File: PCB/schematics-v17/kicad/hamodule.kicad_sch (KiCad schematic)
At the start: 82 parts, among them J1 2604-1104, J10 EspSense, J11 Conn_01x02_Male, J12 NoCon, J2 2604-1102, J3 USB_C_Receptacle_USB2.0, J4 ESP Relays, J5 Current Jumper, J6 GND 3.3V, J7 Conn_01x02, J8 Current Jumper, J9 2604-1104, K1 PCN-105D, K2 PCN-105D, K3 PCN-105D, K4 PCN-105D, Q1 SS8050-SMD, Q2 SS8050, SW1 EN, SW2 IO0, U1 ULN2003A, U2 ESP32-WROOM-32E, U4 LD1117AV33_TO220, U5 MCP9700T-ETT, U6 LDA210-PDIP, U7 LDA210-PDIP, U8 CP2102N-A01-GQFN28

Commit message: adding gerber + BOM + new images for README
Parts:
- R1, R2, R24, R3, R4: footprint Resistor_SMD:R_0603_1608Metric_Pad1.05x0.95mm_HandSolder -> Resistor_SMD:R_0603_1608Metric_Pad0.98x0.95mm_HandSolder
- R5: footprint Resistor_SMD:R_1206_3216Metric_Pad1.42x1.75mm_HandSolder -> Resistor_SMD:R_1206_3216Metric_Pad1.30x1.75mm_HandSolder
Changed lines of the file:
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@@
     (property "Reference" "R24" (id 0) (at 177.8 123.19 90))
     (property "Value" "1kΩ" (id 1) (at 177.8 120.65 90))
-    (property "Footprint" "Resistor_SMD:R_0603_1608Metric_Pad1.05x0.95mm_HandSolder" (id 2) (at 177.8 118.872 90)
+    (property "Footprint" "Resistor_SMD:R_0603_1608Metric_Pad0.98x0.95mm_HandSolder" (id 2) (at 177.8 118.872 90)
       (effects (font (size 1.27 1.27)) hide)
     )
@@
     (property "Reference" "R3" (id 0) (at 219.71 154.94 90))
     (property "Value" "10kΩ" (id 1) (at 219.71 157.48 90))
-    (property "Footprint" "Resistor_SMD:R_0603_1608Metric_Pad1.05x0.95mm_HandSolder" (id 2) (at 219.71 155.702 90)
+    (property "Footprint" "Resistor_SMD:R_0603_1608Metric_Pad0.98x0.95mm_HandSolder" (id 2) (at 219.71 155.702 90)
       (effects (font (size 1.27 1.27)) hide)
     )
@@
     (property "Reference" "R2" (id 0) (at 219.71 140.97 90))
     (property "Value" "10kΩ" (id 1) (at 219.71 143.51 90))
-    (property "Footprint" "Resistor_SMD:R_0603_1608Metric_Pad1.05x0.95mm_HandSolder" (id 2) (at 219.71 141.732 90)
+    (property "Footprint" "Resistor_SMD:R_0603_1608Metric_Pad0.98x0.95mm_HandSolder" (id 2) (at 219.71 141.732 90)
       (effects (font (size 1.27 1.27)) hide)
     )
@@
     (property "Reference" "R1" (id 0) (at 30.48 120.65 90))
     (property "Value" "10kΩ" (id 1) (at 27.94 120.65 90))
-    (property "Footprint" "Resistor_SMD:R_0603_1608Metric_Pad1.05x0.95mm_HandSolder" (id 2) (at 29.718 120.65 90)
+    (property "Footprint" "Resistor_SMD:R_0603_1608Metric_Pad0.98x0.95mm_HandSolder" (id 2) (at 29.718 120.65 90)
       (effects (font (size 1.27 1.27)) hide)
     )
@@
     (property "Reference" "R4" (id 0) (at 144.78 110.49 90))
     (property "Value" "1kΩ" (id 1) (at 144.78 107.95 90))
-    (property "Footprint" "Resistor_SMD:R_0603_1608Metric_Pad1.05x0.95mm_HandSolder" (id 2) (at 144.78 106.172 90)
+    (property "Footprint" "Resistor_SMD:R_0603_1608Metric_Pad0.98x0.95mm_HandSolder" (id 2) (at 144.78 106.172 90)
       (effects (font (size 1.27 1.27)) hide)
     )
@@
     )
     (property "Value" "1kΩ" (id 1) (at 177.8 113.03 90))
-    (property "Footprint" "Resistor_SMD:R_1206_3216Metric_Pad1.42x1.75mm_HandSolder" (id 2) (at 177.8 111.252 90)
+    (property "Footprint" "Resistor_SMD:R_1206_3216Metric_Pad1.30x1.75mm_HandSolder" (id 2) (at 177.8 111.252 90)
       (effects (font (size 1.27 1.27)) hide)
     )
@@
     )
     (path "/00000000-0000-0000-0000-000061ae6949"
-      (reference "R1") (unit 1) (value "10kΩ") (footprint "Resistor_SMD:R_0603_1608Metric_Pad1.05x0.95mm_HandSolder")
+      (reference "R1") (unit 1) (value "10kΩ") (footprint "Resistor_SMD:R_0603_1608Metric_Pad0.98x0.95mm_HandSolder")
     )
     (path "/00000000-0000-0000-0000-000061ae690f"
-      (reference "R2") (unit 1) (value "10kΩ") (footprint "Resistor_SMD:R_0603_1608Metric_Pad1.05x0.95mm_HandSolder")
+      (reference "R2") (unit 1) (value "10kΩ") (footprint "Resistor_SMD:R_0603_1608Metric_Pad0.98x0.95mm_HandSolder")
     )
     (path "/00000000-0000-0000-0000-000061ae6909"
-      (reference "R3") (unit 1) (value "10kΩ") (footprint "Resistor_SMD:R_0603_1608Metric_Pad1.05x0.95mm_HandSolder")
+      (reference "R3") (unit 1) (value "10kΩ") (footprint "Resistor_SMD:R_0603_1608Metric_Pad0.98x0.95mm_HandSolder")
     )
     (path "/00000000-0000-0000-0000-000061caa7bc"
-      (reference "R4") (unit 1) (value "1kΩ") (footprint "Resistor_SMD:R_0603_1608Metric_Pad1.05x0.95mm_HandSolder")
+      (reference "R4") (unit 1) (value "1kΩ") (footprint "Resistor_SMD:R_0603_1608Metric_Pad0.98x0.95mm_HandSolder")
     )
     (path "/00000000-0000-0000-0000-000061db1bb6"
-      (reference "R5") (unit 1) (value "1kΩ") (footprint "Resistor_SMD:R_1206_3216Metric_Pad1.42x1.75mm_HandSolder")
+      (reference "R5") (unit 1) (value "1kΩ") (footprint "Resistor_SMD:R_1206_3216Metric_Pad1.30x1.75mm_HandSolder")
     )
     (path "/00000000-0000-0000-0000-000061db1bc4"
@@
     )
     (path "/00000000-0000-0000-0000-000061ae682e"
-      (reference "R24") (unit 1) (value "1kΩ") (footprint "Resistor_SMD:R_0603_1608Metric_Pad1.05x0.95mm_HandSolder")
+      (reference "R24") (unit 1) (value "1kΩ") (footprint "Resistor_SMD:R_0603_1608Metric_Pad0.98x0.95mm_HandSolder")
     )
     (path "/00000000-0000-0000-0000-00006146aba1"

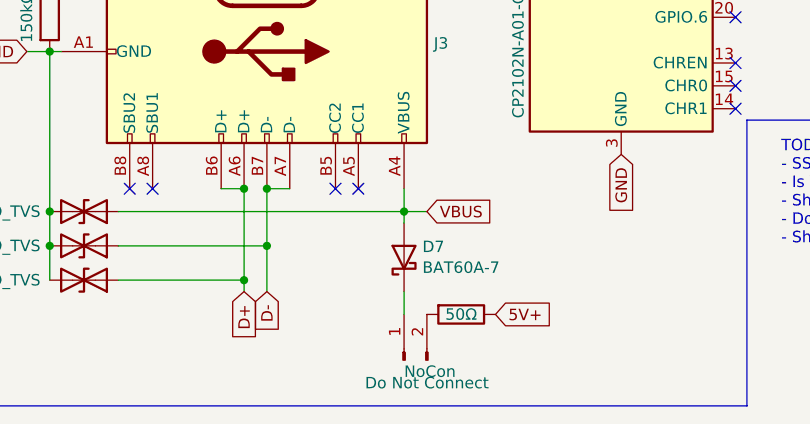
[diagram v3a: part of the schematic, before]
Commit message: adding missing resistors to the USB port
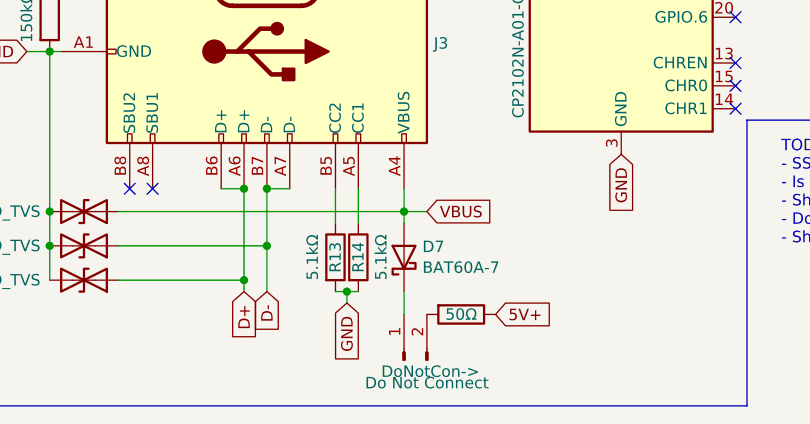
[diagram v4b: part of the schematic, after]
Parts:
- added R13, R14: 5.1kΩ, Resistor_SMD:R_0603_1608Metric_Pad0.98x0.95mm_HandSolder, symbol Device:R
- J12: value NoCon -> DoNotCon->
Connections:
- net GND: now also R13.2, R14.2
- net at J3.A5 (CC1): now also R14.1
- net at J3.B5 (CC2): now also R13.1
- no-connect marks 49 -> 47
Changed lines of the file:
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@@
   (junction (at 120.65 86.36) (diameter 0) (color 0 0 0 0)
   )
+  (junction (at 130.81 184.15) (diameter 0) (color 0 0 0 0)
+  )
   (junction (at 140.97 35.56) (diameter 0) (color 0 0 0 0)
   )
@@
   (no_connect (at 106.68 172.72))
   (no_connect (at 109.22 172.72))
-  (no_connect (at 129.54 172.72))
-  (no_connect (at 132.08 172.72))
   (no_connect (at 173.99 130.81))
   (no_connect (at 67.31 166.37))
@@
     (stroke (width 0) (type default) (color 0 0 0 0))
   )
+  (wire (pts (xy 130.81 184.15) (xy 132.08 184.15))
+    (stroke (width 0) (type default) (color 0 0 0 0))
+  )
   (wire (pts (xy 260.35 59.69) (xy 269.24 59.69))
     (stroke (width 0) (type default) (color 0 0 0 0))
@@
     (stroke (width 0) (type default) (color 0 0 0 0))
   )
+  (wire (pts (xy 130.81 184.15) (xy 130.81 185.42))
+    (stroke (width 0) (type default) (color 0 0 0 0))
+  )
   (wire (pts (xy 26.67 125.73) (xy 27.94 125.73))
     (stroke (width 0) (type default) (color 0 0 0 0))
@@
     (stroke (width 0) (type default) (color 0 0 0 0))
   )
+  (wire (pts (xy 129.54 184.15) (xy 130.81 184.15))
+    (stroke (width 0) (type default) (color 0 0 0 0))
+  )
   (wire (pts (xy 179.07 54.61) (xy 185.42 54.61))
     (stroke (width 0) (type default) (color 0 0 0 0))
@@
     (stroke (width 0) (type default) (color 0 0 0 0))
   )
+  (wire (pts (xy 132.08 172.72) (xy 132.08 176.53))
+    (stroke (width 0) (type default) (color 0 0 0 0))
+  )
   (wire (pts (xy 114.3 76.2) (xy 114.3 81.28))
     (stroke (width 0) (type default) (color 0 0 0 0))
@@
     (stroke (width 0) (type default) (color 0 0 0 0))
   )
+  (wire (pts (xy 129.54 172.72) (xy 129.54 176.53))
+    (stroke (width 0) (type default) (color 0 0 0 0))
+  )
   (polyline (pts (xy 175.26 165.1) (xy 283.21 165.1))
     (stroke (width 0) (type default) (color 0 0 0 0))
@@
     )
   )
+  (global_label "GND" (shape input) (at 130.81 185.42 270) (fields_autoplaced)
+    (effects (font (size 1.27 1.27)) (justify right))
+    (property "Intersheet References" "${INTERSHEET_REFS}" (id 0) (at -7.62 16.51 0)
+      (effects (font (size 1.27 1.27)) hide)
+    )
+  )
   (global_label "GND" (shape input) (at 185.42 54.61 0) (fields_autoplaced)
     (effects (font (size 1.27 1.27)) (justify left))
@@
       (effects (font (size 1.27 1.27)) (justify right) hide)
     )
-    (property "Value" "NoCon" (id 1) (at 137.16 193.04 90)
+    (property "Value" "DoNotCon->" (id 1) (at 134.62 193.04 90)
       (effects (font (size 1.27 1.27)) (justify right))
     )
@@
     (pin "2")
   )
+  (symbol (lib_id "Device:R") (at 129.54 180.34 0) (unit 1)
+    (in_bom yes) (on_board yes)
+    (property "Reference" "R13" (id 0) (at 129.54 180.34 90))
+    (property "Value" "5.1kΩ" (id 1) (at 127 180.34 90))
+    (property "Footprint" "Resistor_SMD:R_0603_1608Metric_Pad0.98x0.95mm_HandSolder" (id 2) (at 127.762 180.34 90)
+      (effects (font (size 1.27 1.27)) hide)
+    )
+    (property "Datasheet" "~" (id 3) (at 129.54 180.34 0)
+      (effects (font (size 1.27 1.27)) hide)
+    )
+    (property "JLCPCB" "C23186" (id 4) (at 129.54 180.34 0)
+      (effects (font (size 1.27 1.27)) hide)
+    )
+    (pin "1")
+    (pin "2")
+  )
+  (symbol (lib_id "Device:R") (at 132.08 180.34 0) (unit 1)
+    (in_bom yes) (on_board yes)
+    (property "Reference" "R14" (id 0) (at 132.08 180.34 90))
+    (property "Value" "5.1kΩ" (id 1) (at 134.62 180.34 90))
+    (property "Footprint" "Resistor_SMD:R_0603_1608Metric_Pad0.98x0.95mm_HandSolder" (id 2) (at 130.302 180.34 90)
+      (effects (font (size 1.27 1.27)) hide)
+    )
+    (property "Datasheet" "~" (id 3) (at 132.08 180.34 0)
+      (effects (font (size 1.27 1.27)) hide)
+    )
+    (property "JLCPCB" "C23186" (id 4) (at 132.08 180.34 0)
+      (effects (font (size 1.27 1.27)) hide)
+    )
+    (pin "1")
+    (pin "2")
+  )
   (symbol (lib_id "Connector:USB_C_Receptacle_USB2.0") (at 121.92 157.48 270) (unit 1)
     (in_bom yes) (on_board yes)
@@
     )
     (path "/00000000-0000-0000-0000-000061e5607b"
-      (reference "J12") (unit 1) (value "NoCon") (footprint "Connector_PinHeader_2.00mm:PinHeader_1x02_P2.00mm_Vertical")
+      (reference "J12") (unit 1) (value "DoNotCon->") (footprint "Connector_PinHeader_2.00mm:PinHeader_1x02_P2.00mm_Vertical")
     )
     (path "/00000000-0000-0000-0000-0000618622ec"
@@
       (reference "R12") (unit 1) (value "150kΩ1w") (footprint "Resistor_SMD:R_2512_6332Metric_Pad1.40x3.35mm_HandSolder")
     )
+    (path "/2f579084-179d-43a4-88b5-9243e1fb8a76"
+      (reference "R13") (unit 1) (value "5.1kΩ") (footprint "Resistor_SMD:R_0603_1608Metric_Pad0.98x0.95mm_HandSolder")
+    )
+    (path "/5210cf7b-1003-4eb3-b3c0-33660c4be3db"
+      (reference "R14") (unit 1) (value "5.1kΩ") (footprint "Resistor_SMD:R_0603_1608Metric_Pad0.98x0.95mm_HandSolder")
+    )
     (path "/00000000-0000-0000-0000-0000613b1e37"

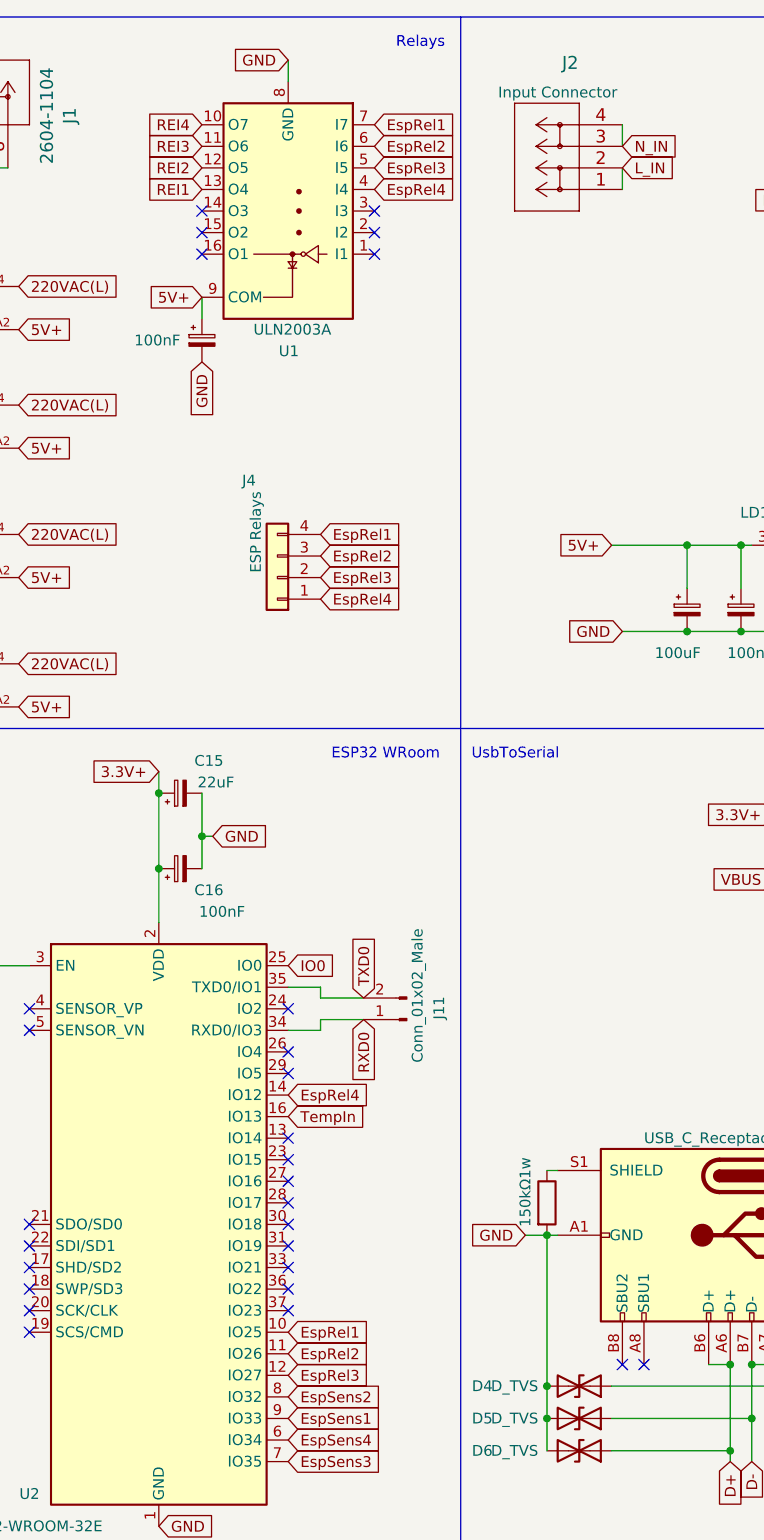
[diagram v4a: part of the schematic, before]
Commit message: fixing EspRel wrong naming
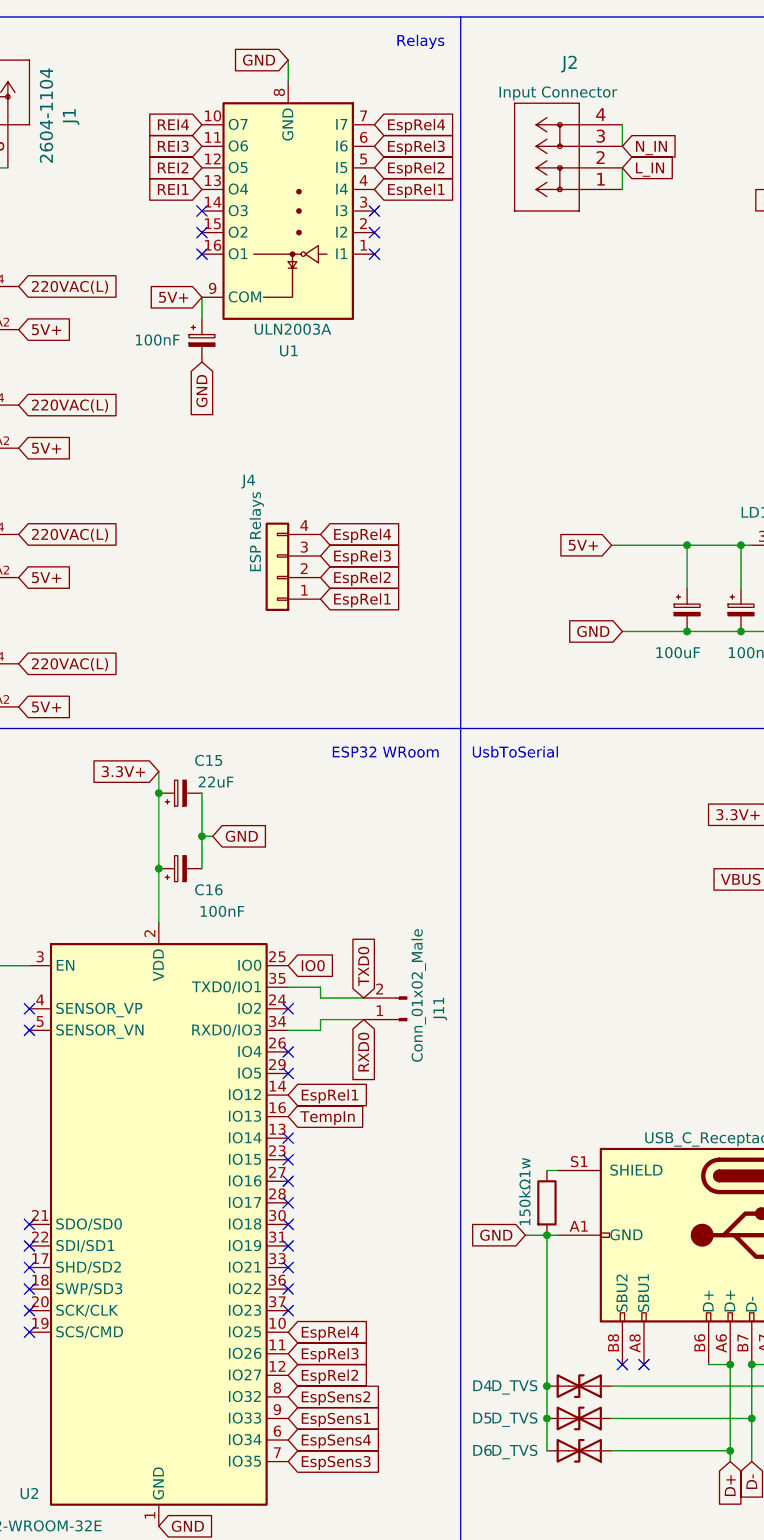
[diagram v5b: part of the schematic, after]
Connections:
- net EspRel1: now also J4.1 (Pin_1), U1.4 (I4), U2.14 (IO12); no longer J4.4 (Pin_4), U1.7 (I7), U2.10 (IO25)
- net EspRel2: now also J4.2 (Pin_2), U1.5 (I5), U2.12 (IO27); no longer J4.3 (Pin_3), U1.6 (I6), U2.11 (IO26)
- net EspRel3: now also J4.3 (Pin_3), U1.6 (I6), U2.11 (IO26); no longer J4.2 (Pin_2), U1.5 (I5), U2.12 (IO27)
- net EspRel4: now also J4.4 (Pin_4), U1.7 (I7), U2.10 (IO25); no longer J4.1 (Pin_1), U1.4 (I4), U2.14 (IO12)
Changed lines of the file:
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@@
     )
   )
-  (global_label "EspRel3" (shape input) (at 71.12 80.01 0) (fields_autoplaced)
+  (global_label "EspRel2" (shape input) (at 71.12 80.01 0) (fields_autoplaced)
     (effects (font (size 1.27 1.27)) (justify left))
     (property "Intersheet References" "${INTERSHEET_REFS}" (id 0) (at 0 0 0)
@@
     )
   )
-  (global_label "EspRel4" (shape input) (at 77.47 34.29 0) (fields_autoplaced)
+  (global_label "EspRel1" (shape input) (at 77.47 34.29 0) (fields_autoplaced)
     (effects (font (size 1.27 1.27)) (justify left))
     (property "Intersheet References" "${INTERSHEET_REFS}" (id 0) (at 0 0 0)
@@
     )
   )
-  (global_label "EspRel1" (shape input) (at 77.47 26.67 0) (fields_autoplaced)
+  (global_label "EspRel4" (shape input) (at 77.47 26.67 0) (fields_autoplaced)
     (effects (font (size 1.27 1.27)) (justify left))
     (property "Intersheet References" "${INTERSHEET_REFS}" (id 0) (at 0 0 0)
@@
     )
   )
-  (global_label "EspRel2" (shape input) (at 71.12 77.47 0) (fields_autoplaced)
-    (effects (font (size 1.27 1.27)) (justify left))
-    (property "Intersheet References" "${INTERSHEET_REFS}" (id 0) (at 0 0 0)
-      (effects (font (size 1.27 1.27)) hide)
-    )
-  )
-  (global_label "EspRel1" (shape input) (at 67.31 168.91 0) (fields_autoplaced)
+  (global_label "EspRel3" (shape input) (at 71.12 77.47 0) (fields_autoplaced)
+    (effects (font (size 1.27 1.27)) (justify left))
+    (property "Intersheet References" "${INTERSHEET_REFS}" (id 0) (at 0 0 0)
+      (effects (font (size 1.27 1.27)) hide)
+    )
+  )
+  (global_label "EspRel4" (shape input) (at 67.31 168.91 0) (fields_autoplaced)
     (effects (font (size 1.27 1.27)) (justify left))
     (property "Intersheet References" "${INTERSHEET_REFS}" (id 0) (at 0 0 0)
@@
     )
   )
-  (global_label "EspRel3" (shape input) (at 77.47 31.75 0) (fields_autoplaced)
+  (global_label "EspRel2" (shape input) (at 77.47 31.75 0) (fields_autoplaced)
     (effects (font (size 1.27 1.27)) (justify left))
     (property "Intersheet References" "${INTERSHEET_REFS}" (id 0) (at 0 0 0)
@@
     )
   )
-  (global_label "EspRel4" (shape input) (at 67.31 140.97 0) (fields_autoplaced)
+  (global_label "EspRel1" (shape input) (at 67.31 140.97 0) (fields_autoplaced)
     (effects (font (size 1.27 1.27)) (justify left))
     (property "Intersheet References" "${INTERSHEET_REFS}" (id 0) (at 0 0 0)
@@
     )
   )
-  (global_label "EspRel2" (shape input) (at 77.47 29.21 0) (fields_autoplaced)
+  (global_label "EspRel3" (shape input) (at 77.47 29.21 0) (fields_autoplaced)
     (effects (font (size 1.27 1.27)) (justify left))
     (property "Intersheet References" "${INTERSHEET_REFS}" (id 0) (at 0 0 0)
@@
     )
   )
-  (global_label "EspRel4" (shape input) (at 71.12 82.55 0) (fields_autoplaced)
+  (global_label "EspRel1" (shape input) (at 71.12 82.55 0) (fields_autoplaced)
     (effects (font (size 1.27 1.27)) (justify left))
     (property "Intersheet References" "${INTERSHEET_REFS}" (id 0) (at 0 0 0)
@@
     )
   )
-  (global_label "EspRel3" (shape input) (at 67.31 173.99 0) (fields_autoplaced)
+  (global_label "EspRel2" (shape input) (at 67.31 173.99 0) (fields_autoplaced)
     (effects (font (size 1.27 1.27)) (justify left))
     (property "Intersheet References" "${INTERSHEET_REFS}" (id 0) (at 0 0 0)
@@
     )
   )
-  (global_label "EspRel2" (shape input) (at 67.31 171.45 0) (fields_autoplaced)
+  (global_label "EspRel3" (shape input) (at 67.31 171.45 0) (fields_autoplaced)
     (effects (font (size 1.27 1.27)) (justify left))
     (property "Intersheet References" "${INTERSHEET_REFS}" (id 0) (at 0 0 0)
@@
     )
   )
-  (global_label "EspRel1" (shape input) (at 71.12 74.93 0) (fields_autoplaced)
-    (effects (font (size 1.27 1.27)) (justify left))
-    (property "Intersheet References" "${INTERSHEET_REFS}" (id 0) (at 0 0 0)
+  (global_label "EspRel4" (shape input) (at 71.12 74.93 0) (fields_autoplaced)
+    (effects (font (size 1.27 1.27)) (justify left))
+    (property "Intersheet References" "${INTERSHEET_REFS}" (id 0) (at 0 0 0)
